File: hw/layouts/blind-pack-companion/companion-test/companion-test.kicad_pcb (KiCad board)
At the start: 2 copper layers, 10 parts

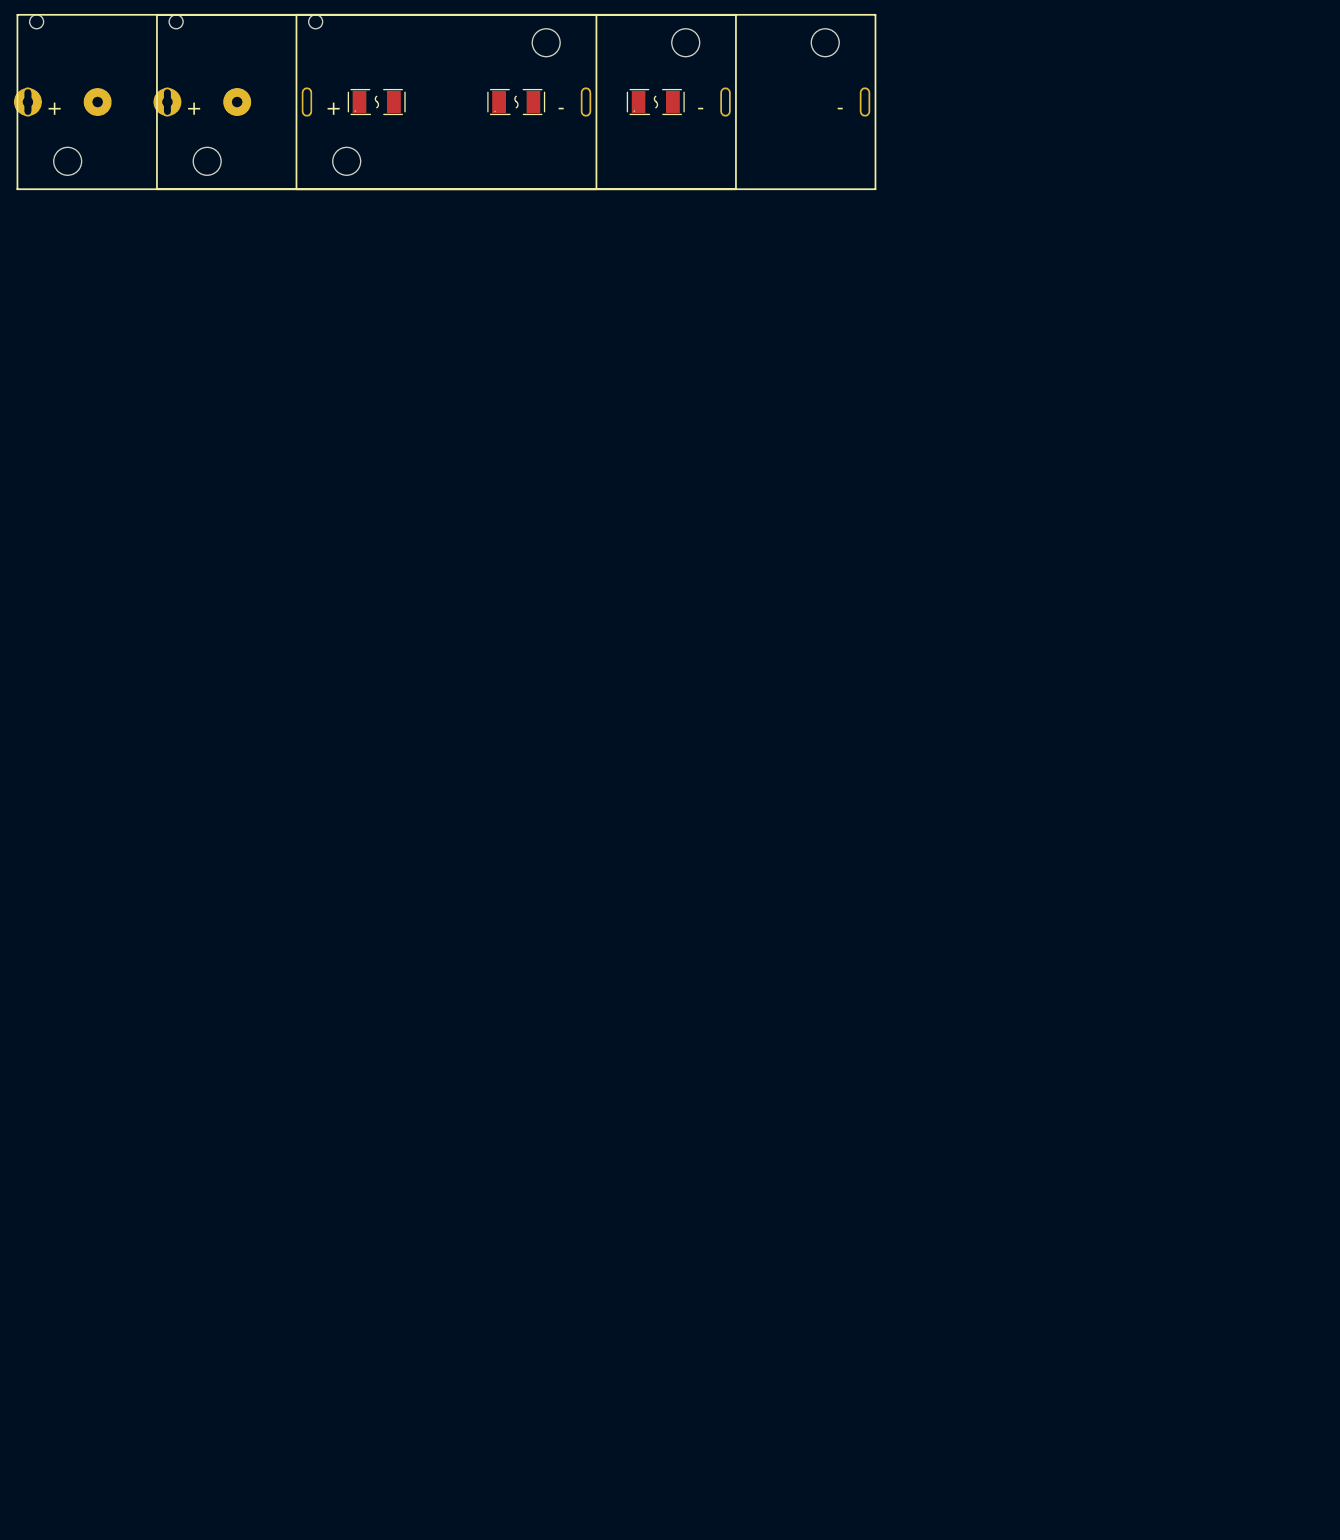
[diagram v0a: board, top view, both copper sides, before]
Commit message: Publish complete controller schematic and retained carrier placements
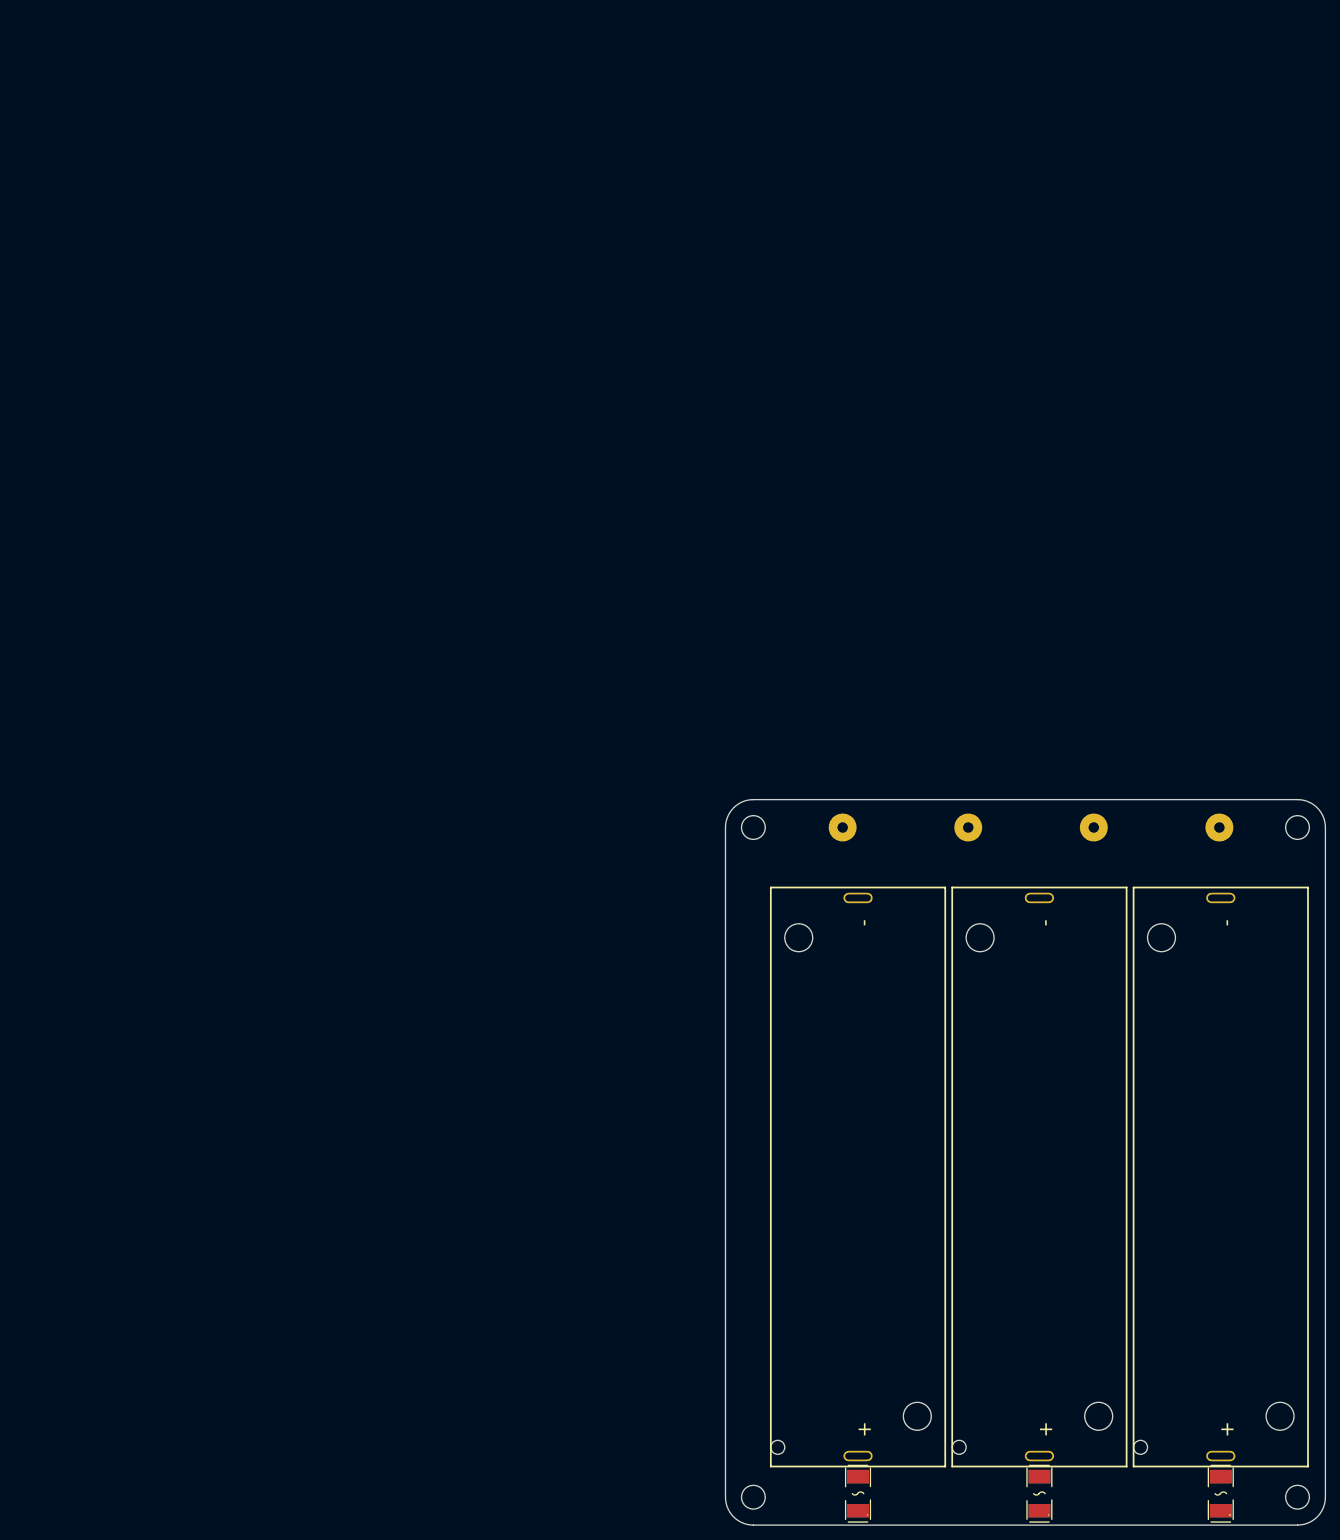
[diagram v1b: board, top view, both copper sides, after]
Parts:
- added H1: M3 clearance 3.4 mm, blind-pack-features:MountingHole_M3_3.4mm, F.Cu at (182.0, 200.0)
- added H2: M3 clearance 3.4 mm, blind-pack-features:MountingHole_M3_3.4mm, F.Cu at (104.0, 200.0)
- added H3: M3 clearance 3.4 mm, blind-pack-features:MountingHole_M3_3.4mm, F.Cu at (182.0, 104.0)
- added H4: M3 clearance 3.4 mm, blind-pack-features:MountingHole_M3_3.4mm, F.Cu at (104.0, 104.0)
- moved F1 233.3 mm to (171.0, 199.5), turned to 90 degrees
- moved F2 213.1 mm to (145.0, 199.5), turned to 90 degrees
- moved BT1 202.3 mm to (171.0, 154.1), turned to 90 degrees
- moved F3 201.6 mm to (119.0, 199.5), turned to 90 degrees
- moved TP3 200.0 mm to (170.8, 104.0)
- moved TP1 176.7 mm to (152.8, 104.0)
- moved BT2 176.0 mm to (145.0, 154.1), turned to 90 degrees
- moved BT3 159.0 mm to (119.0, 154.1), turned to 90 degrees
- moved TP2 154.9 mm to (134.8, 104.0)
- moved TP4 135.5 mm to (116.8, 104.0)
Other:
- board outline added: 86 x 104 mm

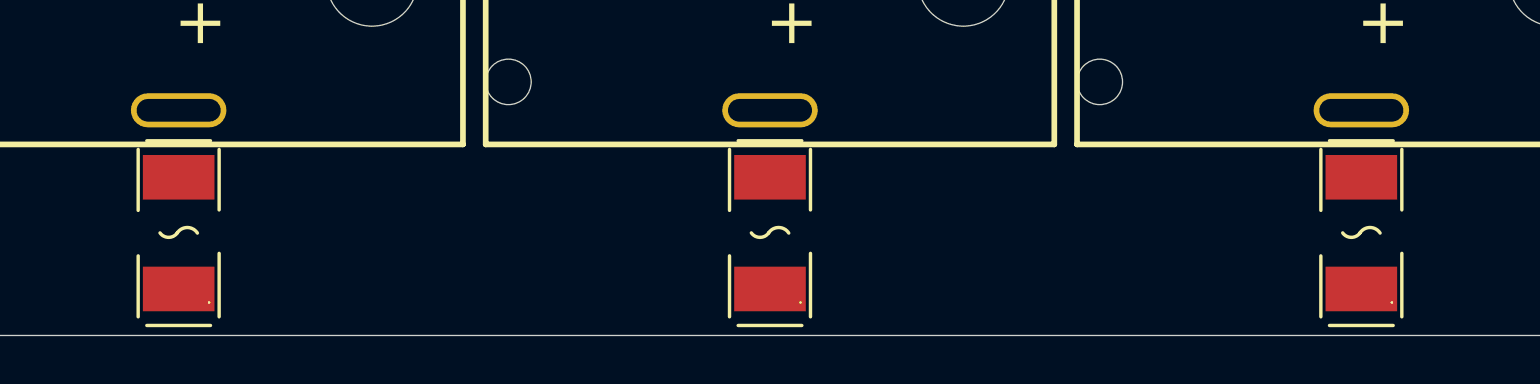
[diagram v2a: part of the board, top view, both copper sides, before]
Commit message: Fix inherited package clearances and repack all three boards
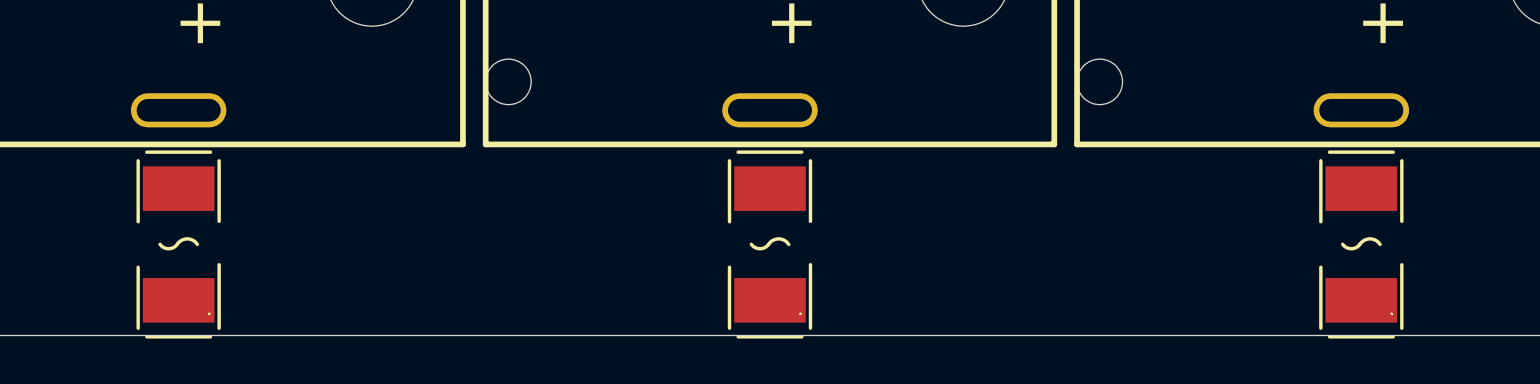
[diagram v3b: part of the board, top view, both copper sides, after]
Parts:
- moved F1 0.50 mm to (171.0, 200.0)
- moved F2 0.50 mm to (145.0, 200.0)
- moved F3 0.50 mm to (119.0, 200.0)
